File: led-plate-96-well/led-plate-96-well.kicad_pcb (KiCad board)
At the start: 4 copper layers, 156.8 x 110.7 mm, 121 parts, among them J1 RAPC722X, U1 A000053, U2 TLC5947RHB, U3 TLC5947RHB, U4 TLC5947RHB, U5 TLC5947RHB

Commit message: start redesign as 2 layer board
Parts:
- C3: value 100uF -> 10uF; footprint Capacitor_SMD:C_1206_3216Metric -> Capacitor_SMD:C_0805_2012Metric
- R1: footprint Resistor_SMD:R_0402_1005Metric -> Resistor_SMD:R_0603_1608Metric
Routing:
- net +5V: track 347.6 -> 0.00 mm, vias 106 -> 0
- net Net-(U1-9(PWM)/A9): track 220.4 -> 0.00 mm, vias 4 -> 0
- net Net-(U1-6(PWM)/A7): track 218.0 -> 0.00 mm, vias 4 -> 0
- net Net-(U1-5(PWM)): track 190.1 -> 0.00 mm, vias 4 -> 0
- net GND: track 105.7 -> 6.50 mm, vias 49 -> 36
- net Net-(U1-3(PWM)/SCL): track 94.1 -> 0.00 mm
- net Net-(U4-SOUT): track 23.5 -> 0.00 mm
- net Net-(U3-SOUT): track 23.5 -> 0.00 mm
- net Net-(U2-SOUT): track 23.5 -> 0.00 mm
- net Net-(U5-IREF): track 5.03 -> 0.00 mm
- net Net-(U4-IREF): track 4.98 -> 0.00 mm
- net Net-(U3-IREF): track 4.98 -> 0.00 mm
- net Net-(U2-IREF): track 4.47 -> 0.00 mm
- removed copper zone on In2.Cu, net +5V
- removed copper zone on In1.Cu, net GND
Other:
- copper layers 4 -> 2

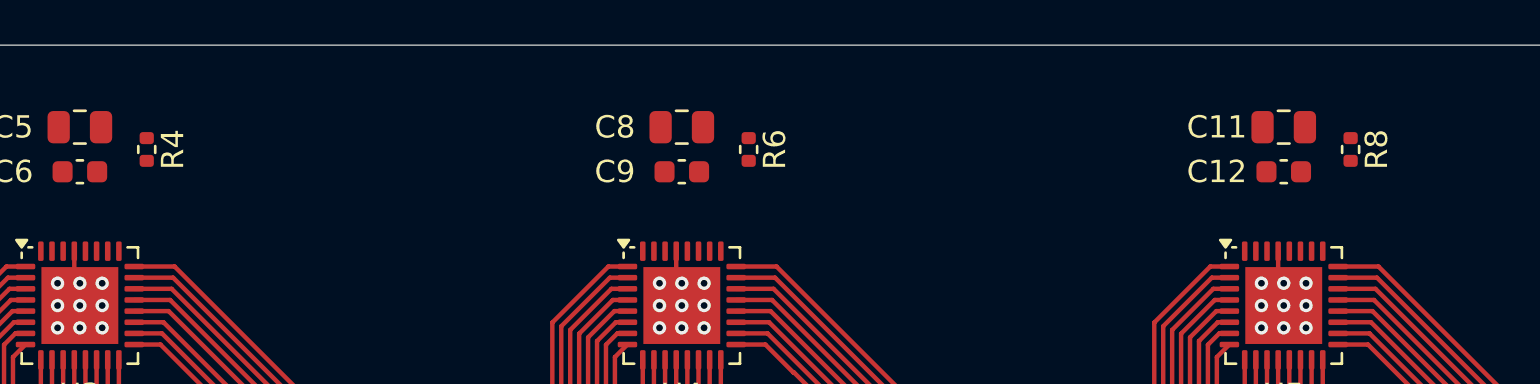
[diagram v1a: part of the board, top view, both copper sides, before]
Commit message: fix some part numbers and footprints
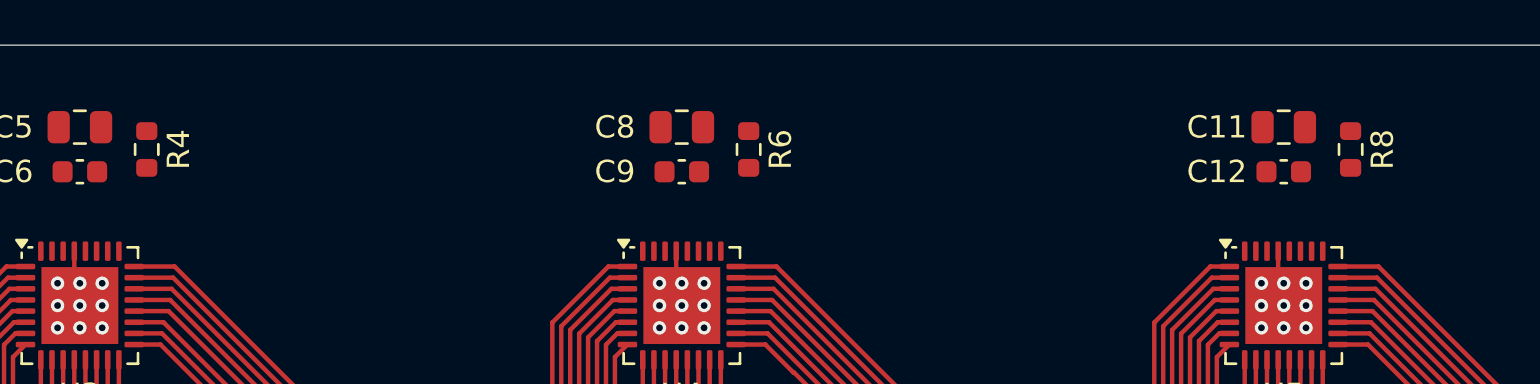
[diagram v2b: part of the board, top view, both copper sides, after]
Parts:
- R4, R6, R8: footprint Resistor_SMD:R_0402_1005Metric -> Resistor_SMD:R_0603_1608Metric
